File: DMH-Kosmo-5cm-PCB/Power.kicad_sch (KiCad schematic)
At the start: 14 parts, among them J0 Conn_01x01, J100 IDC_02x05, J101 IDC_02x08

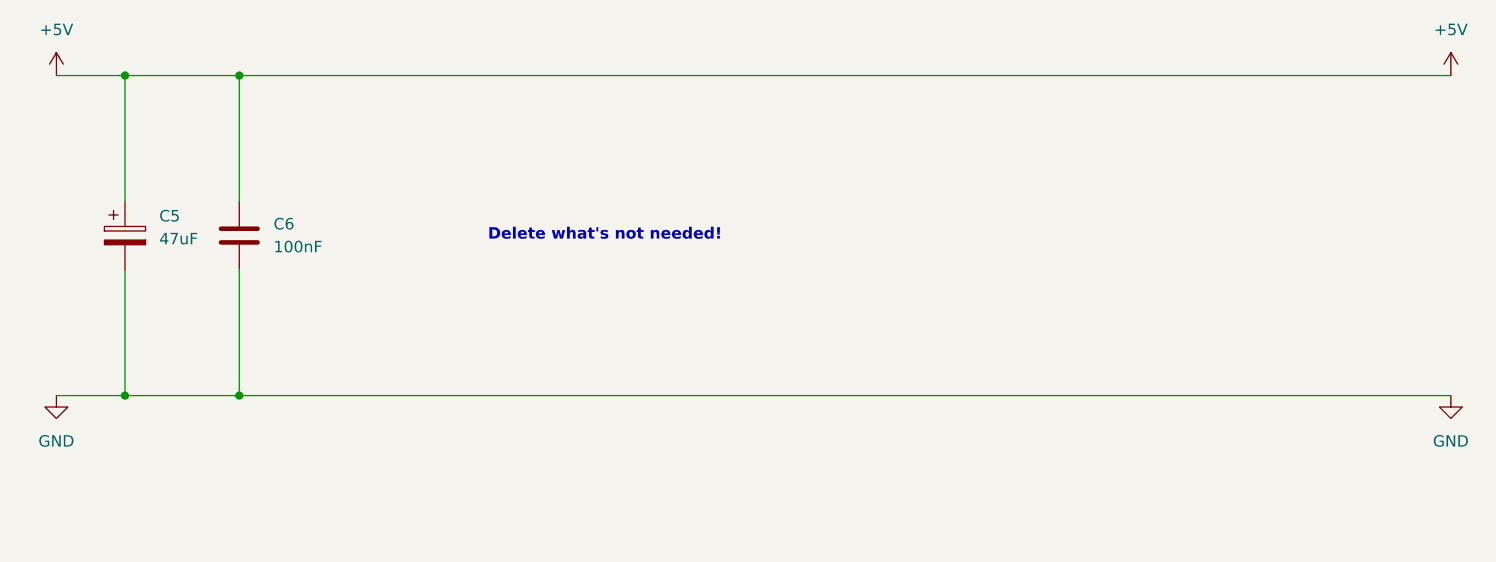
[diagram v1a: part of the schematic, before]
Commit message: Enlarged PCB limits
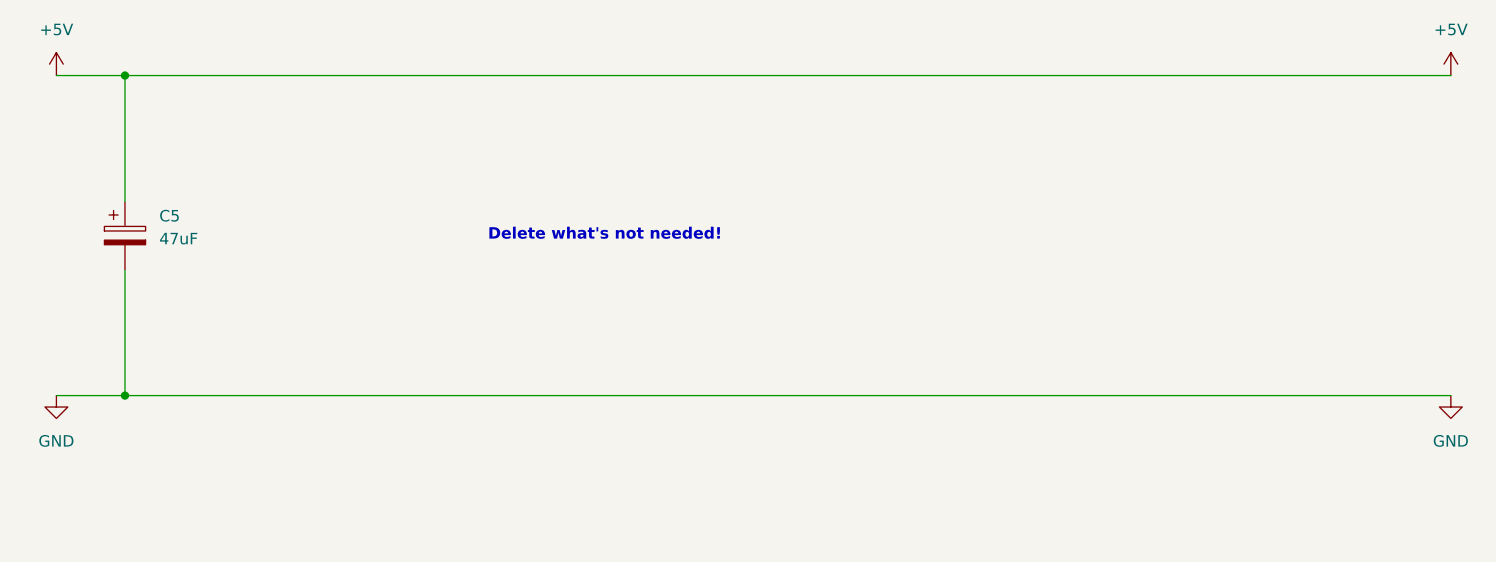
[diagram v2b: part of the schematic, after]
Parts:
- removed C6: 100nF, Capacitor_THT:C_Disc_D4.3mm_W1.9mm_P5.00mm, symbol Device:C
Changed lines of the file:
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@@
 	)
 	(junction
-		(at 38.1 55.88)
-		(diameter 0)
-		(color 0 0 0 0)
-	)
-	(junction
 		(at 33.02 193.04)
 		(diameter 0)
@@
 	)
 	(junction
-		(at 38.1 20.32)
-		(diameter 0)
-		(color 0 0 0 0)
-	)
-	(junction
 		(at 97.79 182.88)
 		(diameter 0)
@@
 	(wire
 		(pts
-			(xy 38.1 20.32) (xy 172.72 20.32)
+			(xy 25.4 20.32) (xy 172.72 20.32)
 		)
 		(stroke
@@
 	(wire
 		(pts
-			(xy 25.4 55.88) (xy 38.1 55.88)
-		)
-		(stroke
-			(width 0)
-			(type default)
-		)
-	)
-	(wire
-		(pts
 			(xy 34.29 165.1) (xy 34.29 185.42)
 		)
@@
 	(wire
 		(pts
-			(xy 38.1 20.32) (xy 38.1 34.29)
-		)
-		(stroke
-			(width 0)
-			(type default)
-		)
-	)
-	(wire
-		(pts
 			(xy 38.1 146.05) (xy 172.72 146.05)
 		)
@@
 	(wire
 		(pts
-			(xy 38.1 41.91) (xy 38.1 55.88)
-		)
-		(stroke
-			(width 0)
-			(type default)
-		)
-	)
-	(wire
-		(pts
-			(xy 25.4 20.32) (xy 38.1 20.32)
-		)
-		(stroke
-			(width 0)
-			(type default)
-		)
-	)
-	(wire
-		(pts
 			(xy 34.29 190.5) (xy 34.29 196.85)
 		)
@@
 	(wire
 		(pts
-			(xy 38.1 55.88) (xy 172.72 55.88)
+			(xy 25.4 55.88) (xy 172.72 55.88)
 		)
 		(stroke
@@
 					(unit 1)
 				)
-			)
-		)
-	)
-	(symbol
-		(lib_id "Device:C")
-		(at 38.1 38.1 0)
-		(unit 1)
-		(body_style 1)
-		(exclude_from_sim no)
-		(in_bom yes)
-		(on_board yes)
-		(in_pos_files yes)
-		(dnp no)
-		(fields_autoplaced yes)
-		(property "Reference" "C6"
-			(at 41.91 36.8299 0)
-			(show_name no)
-			(do_not_autoplace no)
-			(effects
-				(font
-					(size 1.27 1.27)
-				)
-				(justify left)
-			)
-		)
-		(property "Value" "100nF"
-			(at 41.91 39.3699 0)
-			(show_name no)
-			(do_not_autoplace no)
-			(effects
-				(font
-					(size 1.27 1.27)
-				)
-				(justify left)
-			)
-		)
-		(property "Footprint" "Capacitor_THT:C_Disc_D4.3mm_W1.9mm_P5.00mm"
-			(at 39.0652 41.91 0)
-			(hide yes)
-			(show_name no)
-			(do_not_autoplace no)
-			(effects
-				(font
-					(size 1.27 1.27)
-				)
-			)
-		)
-		(property "Datasheet" ""
-			(at 38.1 38.1 0)
-			(hide yes)
-			(show_name no)
-			(do_not_autoplace no)
-			(effects
-				(font
-					(size 1.27 1.27)
-				)
-			)
-		)
-		(property "Description" "Unpolarized capacitor"
-			(at 38.1 38.1 0)
-			(hide yes)
-			(show_name no)
-			(do_not_autoplace no)
-			(effects
-				(font
-					(size 1.27 1.27)
-				)
-			)
-		)
-		(pin "2"
-		)
-		(pin "1"
-		)
-		(instances
-			(project "DMH-Kosmo-5cm-PCB"
-				(path "/58f4306d-5387-4983-bb08-41a2313fd315/0cdf34b2-39cd-4d9e-981a-97cd34791509"
-					(reference "C6")
-					(unit 1)
-				)
